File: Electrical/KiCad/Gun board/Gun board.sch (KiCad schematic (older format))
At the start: 63 parts, among them J2 Conn_01x05, Q1 2N3904, Q3 2N3904, Q4 2N3904, SW1 SW_SPST, SW2 SW_SPST, U1 AAT1217, U2 AMS1117, U3 M25PX32-VMW, U4 MCP4725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

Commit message: finished schematic, working on laying out pcb
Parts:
- removed C?: 10μF, symbol Device:CP
- removed R12: 1.02MΩ, symbol Device:R
- removed R13: 332kΩ, symbol Device:R
- removed R17: 10kΩ, symbol Device:R
- added C15: 10nF, symbol Device:C
- added R12: 1MΩ, symbol Device:R_Small
- added R13: 330kΩ, symbol Device:R_Small
- added R14: 20kΩ, symbol Device:R_Small
- added R17: 2kΩ, symbol Device:R_Small
- C11: value 50nF -> 47nF
- R4: value 180kΩ -> 150kΩ
- gave numbers to parts that had none: 3
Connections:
- wire segments 109 -> 110
- no-connect marks 3 -> 7
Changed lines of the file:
@@
 Wire Wire Line
 	1100 1550 1300 1550
-Wire Wire Line
-	2450 1250 3000 1250
 $Comp
 L Device:D_Schottky D1
@@
 Wire Wire Line
 	1700 1850 1700 1700
-$Comp
-L Device:R R13
-U 1 1 5CB4682D
-P 2450 1700
-F 0 "R13" H 2520 1746 50  0000 L CNN
-F 1 "332kΩ" H 2520 1655 50  0000 L CNN
-F 2 "" V 2380 1700 50  0001 C CNN
-F 3 "~" H 2450 1700 50  0001 C CNN
-	1    2450 1700
-	1    0    0    -1
-$EndComp
-$Comp
-L Device:R R12
-U 1 1 5CB3FC97
-P 2450 1400
-F 0 "R12" H 2520 1446 50  0000 L CNN
-F 1 "1.02MΩ" H 2520 1355 50  0000 L CNN
-F 2 "" V 2380 1400 50  0001 C CNN
-F 3 "~" H 2450 1400 50  0001 C CNN
-	1    2450 1400
-	1    0    0    -1
-$EndComp
 Wire Wire Line
 	2000 800  2100 800
@@
 	9350 800  9700 800
 Wire Wire Line
-	5750 1150 5850 1150
-Wire Wire Line
-	5750 1250 5850 1250
-Wire Wire Line
-	5750 1350 5850 1350
-Wire Wire Line
-	5750 1450 5850 1450
-Wire Wire Line
 	5750 1550 5850 1550
 Wire Wire Line
@@
 	0    -1   -1   0
 $EndComp
-Text Label 6700 5900 2    50   ~ 0
+Text Label 6650 5900 2    50   ~ 0
 LED1
 $Comp
@@
 $EndComp
 Connection ~ 600  1250
-Wire Wire Line
-	4450 1650 4450 2450
 Wire Wire Line
 	4450 1350 4750 1350
@@
 F 3 "" H 4450 2500 50  0001 C CNN
 	1    4450 2500
-	1    0    0    -1
-$EndComp
-$Comp
-L Device:R R17
-U 1 1 5CB83812
-P 4450 1500
-F 0 "R17" H 4520 1546 50  0000 L CNN
-F 1 "10kΩ" H 4520 1455 50  0000 L CNN
-F 2 "" V 4380 1500 50  0001 C CNN
-F 3 "~" H 4450 1500 50  0001 C CNN
-	1    4450 1500
 	1    0    0    -1
 $EndComp
@@
 P 5200 4350
 F 0 "C11" H 5315 4396 50  0000 L CNN
-F 1 "50nF" H 5315 4305 50  0000 L CNN
+F 1 "47nF" H 5315 4305 50  0000 L CNN
 F 2 "" H 5238 4200 50  0001 C CNN
 F 3 "~" H 5200 4350 50  0001 C CNN
@@
 $EndComp
 Wire Wire Line
-	2450 1850 1700 1850
-Wire Wire Line
 	600  1250 1100 1250
 Wire Wire Line
@@
 Wire Wire Line
 	2100 800  2100 1250
-Wire Wire Line
-	2100 1250 2450 1250
 Connection ~ 2100 1250
-Wire Wire Line
-	2100 1550 2450 1550
-Connection ~ 2450 1550
-Connection ~ 2450 1250
 $Comp
 L Transistor_BJT:2N3904 Q1
@@
 P 3900 4000
 F 0 "R4" H 3959 4046 50  0000 L CNN
-F 1 "180kΩ" H 3959 3955 50  0000 L CNN
+F 1 "150kΩ" H 3959 3955 50  0000 L CNN
 F 2 "" H 3900 4000 50  0001 C CNN
 F 3 "~" H 3900 4000 50  0001 C CNN
@@
 Wire Wire Line
 	3350 4000 3500 4000
-$Comp
-L Device:CP C?
-U 1 1 5CF78881
-P 3650 4000
-F 0 "C?" V 3905 4000 50  0000 C CNN
-F 1 "10μF" V 3814 4000 50  0000 C CNN
-F 2 "" H 3688 3850 50  0001 C CNN
-F 3 "~" H 3650 4000 50  0001 C CNN
-	1    3650 4000
-	0    -1   -1   0
-$EndComp
 Wire Wire Line
 	4950 5450 5000 5450
@@
 	4650 5450 4600 5450
 $Comp
-L Device:C C?
+L Device:C C16
 U 1 1 5CFA7ED9
 P 3750 7250
-F 0 "C?" H 3865 7296 50  0000 L CNN
+F 0 "C16" H 3865 7296 50  0000 L CNN
 F 1 "100nF" H 3865 7205 50  0000 L CNN
 F 2 "" H 3788 7100 50  0001 C CNN
@@
 $EndComp
 $Comp
-L power:+3.3V #PWR?
+L power:+3.3V #PWR015
 U 1 1 5CFAC6BA
 P 3750 7100
-F 0 "#PWR?" H 3750 6950 50  0001 C CNN
+F 0 "#PWR015" H 3750 6950 50  0001 C CNN
 F 1 "+3.3V" H 3765 7273 50  0000 C CNN
 F 2 "" H 3750 7100 50  0001 C CNN
@@
 $EndComp
 $Comp
-L Gun-board-rescue:GND-custom_power #PWR?
+L Gun-board-rescue:GND-custom_power #PWR036
 U 1 1 5CFB03DC
 P 3750 7400
-F 0 "#PWR?" H 3750 7150 50  0001 C CNN
+F 0 "#PWR036" H 3750 7150 50  0001 C CNN
 F 1 "GND" H 3755 7227 50  0000 C CNN
 F 2 "" H 3750 7400 50  0001 C CNN
@@
 $EndComp
 $Comp
-L Device:CP C?
+L Device:CP C18
 U 1 1 5CFC18AE
 P 8600 4000
-F 0 "C?" H 8718 4046 50  0000 L CNN
+F 0 "C18" H 8718 4046 50  0000 L CNN
 F 1 "4.7μF" H 8718 3955 50  0000 L CNN
 F 2 "" H 8638 3850 50  0001 C CNN
@@
 $EndComp
 $Comp
-L Device:C C?
+L Device:C C17
 U 1 1 5CFC5656
 P 8100 4000
-F 0 "C?" H 8215 4046 50  0000 L CNN
+F 0 "C17" H 8215 4046 50  0000 L CNN
 F 1 "100nF" H 8215 3955 50  0000 L CNN
 F 2 "" H 8138 3850 50  0001 C CNN
@@
 Connection ~ 7500 4150
 $Comp
-L power:+3.3V #PWR?
+L power:+3.3V #PWR038
 U 1 1 5D032B21
 P 8600 3850
-F 0 "#PWR?" H 8600 3700 50  0001 C CNN
+F 0 "#PWR038" H 8600 3700 50  0001 C CNN
 F 1 "+3.3V" V 8550 4050 50  0000 C CNN
 F 2 "" H 8600 3850 50  0001 C CNN
@@
 $EndComp
 $Comp
-L power:+3.3V #PWR?
+L power:+3.3V #PWR037
 U 1 1 5D06DBB1
 P 5900 7100
-F 0 "#PWR?" H 5900 6950 50  0001 C CNN
+F 0 "#PWR037" H 5900 6950 50  0001 C CNN
 F 1 "+3.3V" V 5915 7273 50  0000 C CNN
 F 2 "" H 5900 7100 50  0001 C CNN
@@
 Text Notes 9750 3100 0    50   ~ 0
 POWER SWITCH
+Wire Wire Line
+	4450 1350 4450 2450
+$Comp
+L Device:C C15
+U 1 1 5D937163
+P 3650 4000
+F 0 "C15" H 3765 4046 50  0000 L CNN
+F 1 "10nF" H 3765 3955 50  0000 L CNN
+F 2 "" H 3688 3850 50  0001 C CNN
+F 3 "~" H 3650 4000 50  0001 C CNN
+	1    3650 4000
+	0    -1   -1   0
+$EndComp
+NoConn ~ 5750 1150
+NoConn ~ 5750 1250
+NoConn ~ 5750 1350
+NoConn ~ 5750 1450
+$Comp
+L Device:R_Small R14
+U 1 1 5D97AF76
+P 2450 1400
+F 0 "R14" H 2509 1446 50  0000 L CNN
+F 1 "20kΩ" H 2509 1355 50  0000 L CNN
+F 2 "" H 2450 1400 50  0001 C CNN
+F 3 "~" H 2450 1400 50  0001 C CNN
+	1    2450 1400
+	0    -1   -1   0
+$EndComp
+$Comp
+L Device:R_Small R12
+U 1 1 5D97ECDC
+P 2250 1400
+F 0 "R12" H 2309 1446 50  0000 L CNN
+F 1 "1MΩ" H 2309 1355 50  0000 L CNN
+F 2 "" H 2250 1400 50  0001 C CNN
+F 3 "~" H 2250 1400 50  0001 C CNN
+	1    2250 1400
+	0    -1   -1   0
+$EndComp
+$Comp
+L Device:R_Small R17
+U 1 1 5D9A3E44
+P 2450 1750
+F 0 "R17" H 2509 1796 50  0000 L CNN
+F 1 "2kΩ" H 2509 1705 50  0000 L CNN
+F 2 "" H 2450 1750 50  0001 C CNN
+F 3 "~" H 2450 1750 50  0001 C CNN
+	1    2450 1750
+	0    -1   -1   0
+$EndComp
+$Comp
+L Device:R_Small R13
+U 1 1 5D9A3E4B
+P 2250 1750
+F 0 "R13" H 2309 1796 50  0000 L CNN
+F 1 "330kΩ" H 2309 1705 50  0000 L CNN
+F 2 "" H 2250 1750 50  0001 C CNN
+F 3 "~" H 2250 1750 50  0001 C CNN
+	1    2250 1750
+	0    -1   -1   0
+$EndComp
+Wire Wire Line
+	2100 1250 3000 1250
+Wire Wire Line
+	2100 1550 2150 1550
+Wire Wire Line
+	2150 1550 2150 1750
+Wire Wire Line
+	2550 1750 2550 1850
+Wire Wire Line
+	1700 1850 2550 1850
+Wire Wire Line
+	2150 1550 2550 1550
+Wire Wire Line
+	2550 1550 2550 1400
+Connection ~ 2150 1550
+Wire Wire Line
+	2100 1250 2100 1400
+Wire Wire Line
+	2100 1400 2150 1400
 $EndSCHEMATC

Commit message: Started adding footprints to PCB
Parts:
- BT1, LS1, SW1, SW2: footprint (none) -> Connector_JST:JST_PH_S2B-PH-K_1x02_P2.00mm_Horizontal
- C1, C13, C4: footprint (none) -> Capacitor_SMD:CP_Elec_5x5.4
- C10, C18, C2, C5, C8: footprint (none) -> Capacitor_SMD:CP_Elec_4x5.4
- C11, C14, C15, C16, C17, C6, C7, C9: footprint (none) -> Capacitor_SMD:C_0805_2012Metric
- C12: footprint (none) -> Capacitor_SMD:CP_Elec_8x10.5
- C3: footprint (none) -> Capacitor_SMD:CP_Elec_6.3x5.4
- D1: footprint (none) -> Diode_SMD:D_SOD-123
- D2, D3: footprint (none) -> LED_THT:LED_D5.0mm
- J2: footprint (none) -> Connector_PinHeader_2.54mm:PinHeader_1x05_P2.54mm_Vertical
- JP1: footprint (none) -> Connector_PinHeader_2.54mm:PinHeader_1x02_P2.54mm_Vertical
- L1: footprint (none) -> Inductor_SMD:L_10.4x10.4_H4.8
- LD1, LD2, LD3, LD4, LD5: footprint (none) -> Connector_JST:JST_PH_B2B-PH-K_1x02_P2.00mm_Vertical
- R1, R10, R11, R12, R13, R14, R15, R16, R17, R18, R19, R2, R20, R26, R3, R4, R5, R6, R7, R8, R9: footprint (none) -> Resistor_SMD:R_0805_2012Metric
- U1: footprint SOT23-6 -> Package_TO_SOT_SMD:SOT-23-6
- U4: footprint (none) -> Package_TO_SOT_SMD:SOT-23-6
- U8: footprint (none) -> Package_SO:SOIC-8-1EP_3.9x4.9mm_P1.27mm_EP2.29x3mm

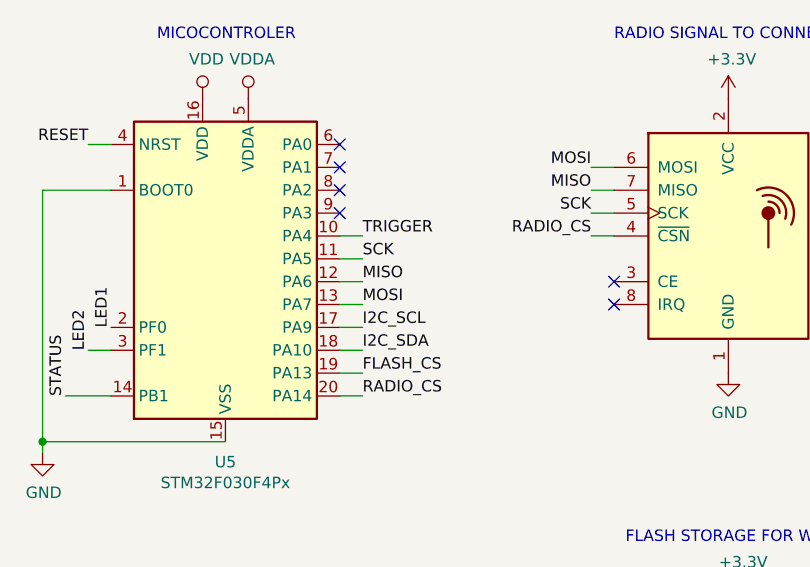
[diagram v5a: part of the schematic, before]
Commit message: power and audio traces routed
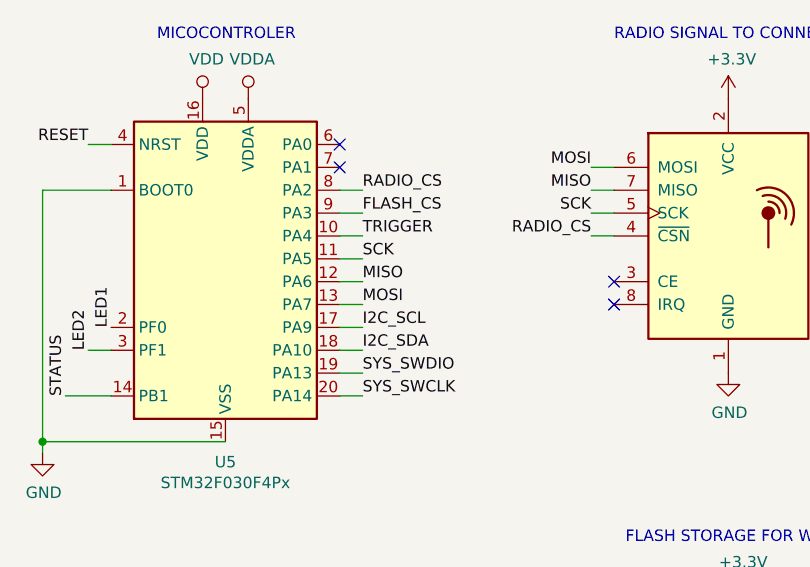
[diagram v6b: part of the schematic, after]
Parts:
- L1: footprint Inductor_SMD:L_10.4x10.4_H4.8 -> Inductor_SMD:L_TracoPower_TCK-141
- U8: footprint Package_SO:SOIC-8-1EP_3.9x4.9mm_P1.27mm_EP2.29x3mm -> Package_SO:SOIC-8_3.9x4.9mm_P1.27mm
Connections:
- net FLASH_CS: now also U5.9 (PA3); no longer U5.19 (PA13)
- net RADIO_CS: now also U5.8 (PA2); no longer U5.20 (PA14)
- net SYS_SWCLK: now also U5.20 (PA14)
- net SYS_SWDIO: now also U5.19 (PA13)
- no-connect marks 7 -> 5
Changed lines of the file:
@@
 EESchema Schematic File Version 4
 LIBS:Gun board-cache
-EELAYER 29 0
+EELAYER 26 0
 EELAYER END
 $Descr USLetter 11000 8500
@@
 F 0 "L1" V 1640 800 50  0000 C CNN
 F 1 "4.7μH" V 1549 800 50  0000 C CNN
-F 2 "Inductor_SMD:L_10.4x10.4_H4.8" H 1450 800 50  0001 C CNN
+F 2 "Inductor_SMD:L_TracoPower_TCK-141" H 1450 800 50  0001 C CNN
 F 3 "~" H 1450 800 50  0001 C CNN
 	1    1450 800
@@
 F 0 "U8" H 5044 4146 50  0000 L CNN
 F 1 "LM386" H 5044 4055 50  0000 L CNN
-F 2 "Package_SO:SOIC-8-1EP_3.9x4.9mm_P1.27mm_EP2.29x3mm" H 4800 4200 50  0001 C CNN
+F 2 "Package_SO:SOIC-8_3.9x4.9mm_P1.27mm" H 4800 4200 50  0001 C CNN
 F 3 "http://www.ti.com/lit/ds/symlink/lm386.pdf" H 4900 4300 50  0001 C CNN
 	1    4700 4100
@@
 Text Label 5850 1550 0    50   ~ 0
 TRIGGER
-Text Label 5850 2150 0    50   ~ 0
+Text Label 5850 1450 0    50   ~ 0
 FLASH_CS
-Text Label 5850 2250 0    50   ~ 0
+Text Label 5850 1350 0    50   ~ 0
 RADIO_CS
 Connection ~ 4100 4000
@@
 NoConn ~ 5750 1150
 NoConn ~ 5750 1250
-NoConn ~ 5750 1350
-NoConn ~ 5750 1450
 $Comp
 L Device:R_Small R14
@@
 Wire Wire Line
 	2100 1400 2150 1400
+Wire Wire Line
+	5750 1350 5850 1350
+Wire Wire Line
+	5750 1450 5850 1450
+Text Label 5850 2150 0    50   ~ 0
+SYS_SWDIO
+Text Label 5850 2250 0    50   ~ 0
+SYS_SWCLK
 $EndSCHEMATC
